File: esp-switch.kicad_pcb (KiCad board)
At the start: 2 copper layers, 23 parts, among them J1 Conn_01x02, J2 Screw_Terminal_01x02, J3 Screw_Terminal_01x02, J4 Conn_01x04, U1 ATTINY441-SSU, U2 ESP-01v090, U3 MOC3041M, U4 MOC3041M

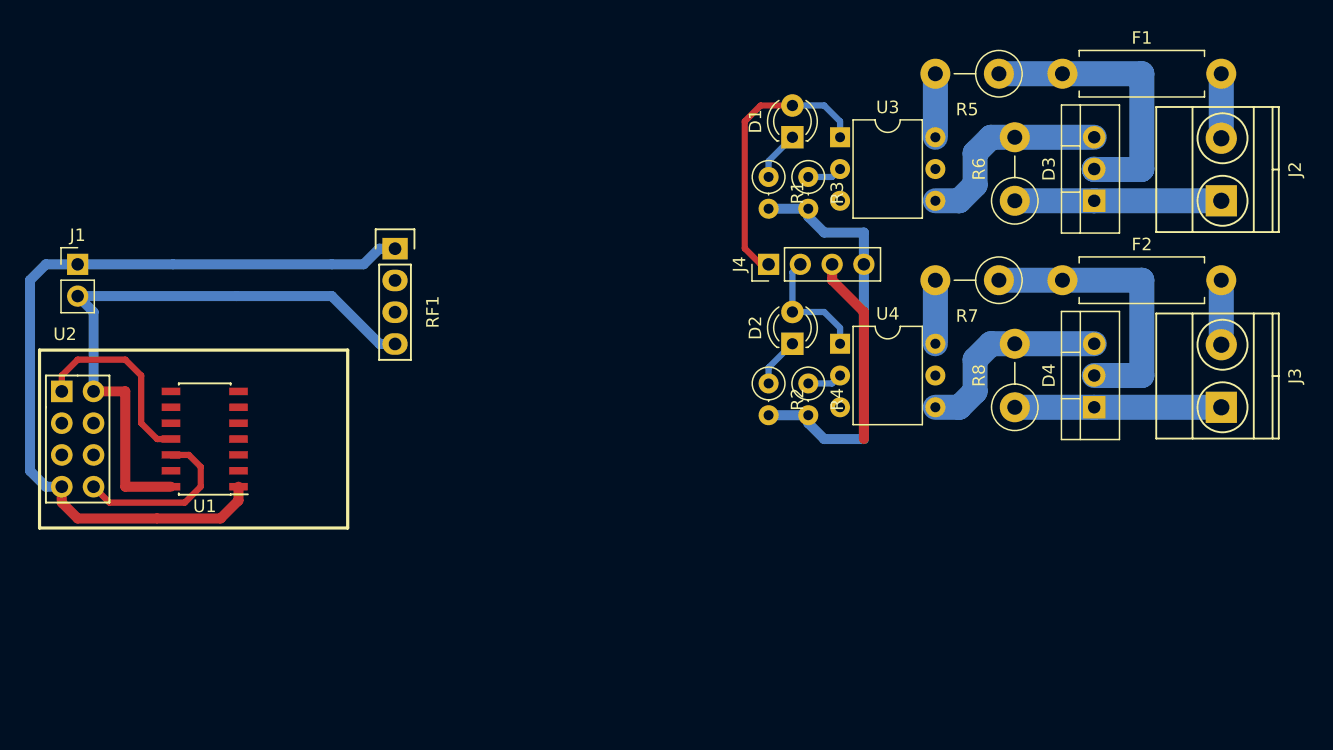
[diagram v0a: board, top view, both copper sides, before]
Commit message: Power supply added
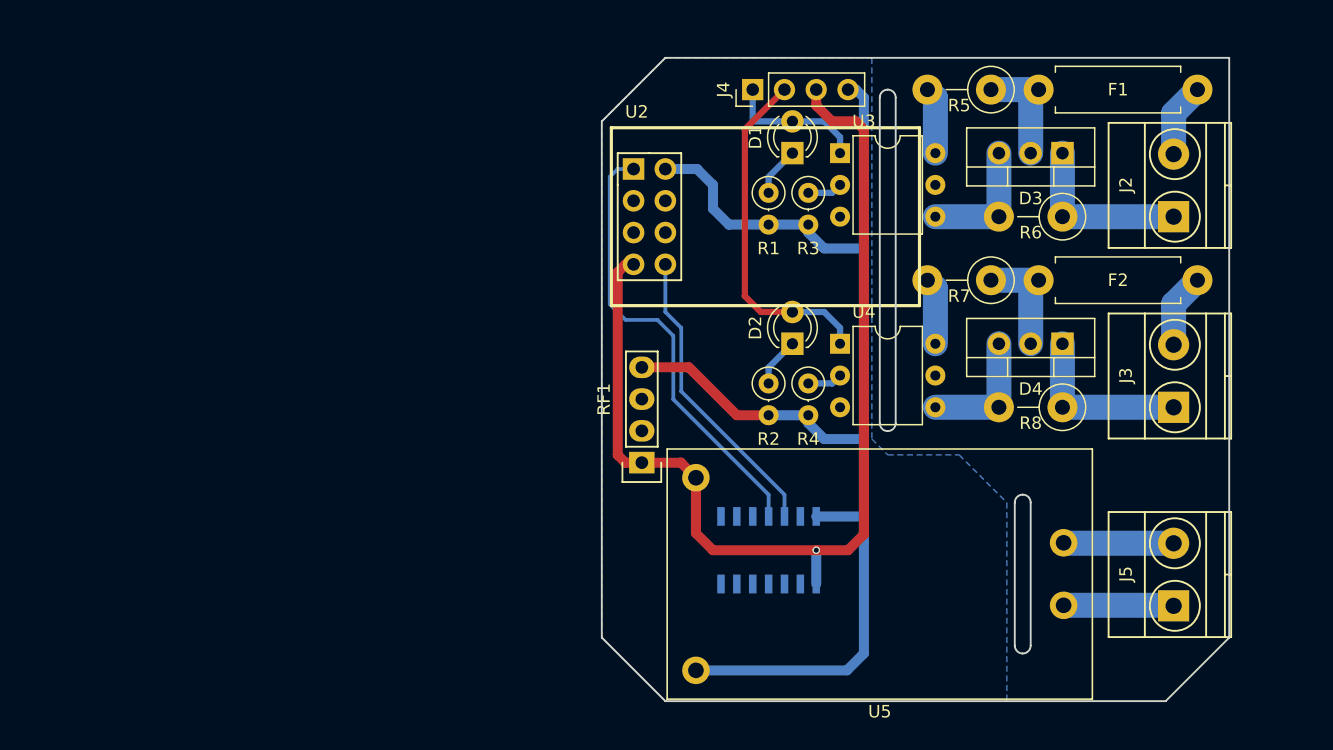
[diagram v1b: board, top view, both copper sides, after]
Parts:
- removed J1: Conn_01x02, Pin_Headers:Pin_Header_Straight_1x02_Pitch2.54mm
- added J5: Screw_Terminal_01x02, Connectors_Terminal_Blocks:TerminalBlock_Pheonix_MKDS1.5-2pol, F.Cu at (219.7, 136.5)
- added U5: HLK-PM05, Power_Supply:HLK-PM05, F.Cu at (196.2, 134.0)
- U1: moved to B.Cu
- moved U2 49.1 mm to (176.5, 101.6)
- moved U1 46.0 mm to (187.3, 132.1), turned to 90 degrees
- moved RF1 20.9 mm to (177.2, 120.0), turned to 90 degrees
- moved J4 14.0 mm to (186.1, 95.2)
- moved D4 5.68 mm to (210.8, 115.6), turned to 180 degrees
- moved D3 4.58 mm to (210.8, 100.3), turned to 180 degrees
- moved J2 4.02 mm to (219.7, 105.4)
- moved R6 4.02 mm to (210.8, 105.4), turned to 180 degrees
- moved J3 3.81 mm to (219.7, 120.7)
- moved R8 3.81 mm to (210.8, 120.7), turned to 180 degrees
- moved F1 2.29 mm to (208.9, 95.2)
- moved F2 1.91 mm to (208.9, 110.5)
- moved R5 1.42 mm to (205.1, 95.2)
- moved D1 1.27 mm to (189.2, 100.3)
- moved R1 1.27 mm to (187.3, 103.5)
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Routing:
- net GND: track 83.0 -> 104.4 mm
- net Net-(U1-Pad11): track 15.7 -> 36.1 mm
- net Net-(D2-Pad2): track 9.68 -> 27.8 mm
- net Net-(D3-Pad2): track 22.9 -> 9.15 mm
- net Net-(D4-Pad2): track 22.9 -> 9.15 mm
- net Net-(D1-Pad2): track 22.5 -> 11.3 mm
- net Net-(U1-Pad12): track 14.0 -> 24.1 mm
- net Net-(J5-Pad2): track 0.00 -> 8.81 mm
- net Net-(J5-Pad1): track 0.00 -> 8.81 mm
- net Net-(D3-Pad3): track 16.3 -> 10.2 mm
- net Net-(D4-Pad3): track 16.3 -> 10.2 mm
- net Net-(D3-Pad1): track 16.5 -> 14.0 mm
- net Net-(D4-Pad1): track 16.5 -> 14.0 mm
- net +5V: track 81.2 -> 83.1 mm, vias 0 -> 1
- net Net-(F2-Pad2): track 5.16 -> 5.95 mm
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- added copper zone on B.Cu, net GND
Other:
- board outline added: 50.2 x 51.4 mm
- net class Default: clearance 0.3 -> 0.2; trace_width 0.5 -> 0.3
- rule trace_clearance: 0.3 -> 0.2

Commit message: Single switch source
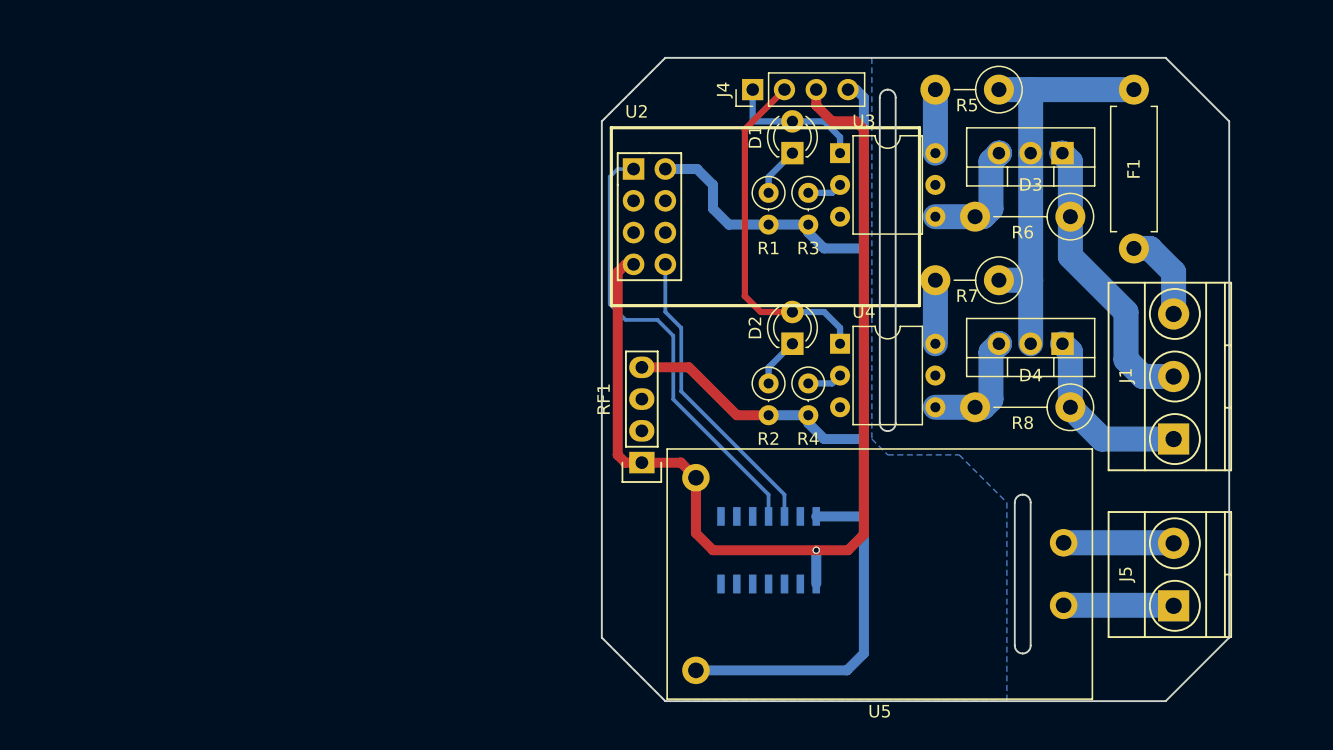
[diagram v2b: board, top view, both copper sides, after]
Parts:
- removed F2: Fuse_Small, Resistors_THT:R_Axial_DIN0411_L9.9mm_D3.6mm_P12.70mm_Horizontal
- removed J2, J3: Screw_Terminal_01x02, Connectors_Terminal_Blocks:TerminalBlock_Pheonix_MKDS1.5-2pol
- added J1: Screw_Terminal_01x03, Connectors_Terminal_Blocks:TerminalBlock_Pheonix_MKDS1.5-3pol, F.Cu at (219.7, 123.2)
- R6, R8: footprint Resistors_THT:R_Axial_DIN0411_L9.9mm_D3.6mm_P5.08mm_Vertical -> Resistors_THT:R_Axial_DIN0411_L9.9mm_D3.6mm_P7.62mm_Vertical
- moved F1 7.62 mm to (216.5, 95.2), turned to 270 degrees
- moved R5 0.64 mm to (205.7, 95.2)
- moved R6 0.64 mm to (211.5, 105.4)
- moved R7 0.64 mm to (205.7, 110.5)
- moved R8 0.64 mm to (211.5, 120.7)
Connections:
- D4 pad 2: Net-(D4-Pad2) -> Net-(D3-Pad2)
- R7 pad 1: Net-(D4-Pad2) -> Net-(D3-Pad2)
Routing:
- net Net-(D3-Pad2): track 9.15 -> 33.7 mm
- net Net-(D4-Pad2): track 9.15 -> 0.00 mm
- net Net-(D3-Pad1): track 14.0 -> 23.0 mm
- net Net-(F2-Pad2): track 5.95 -> 0.00 mm
- net Net-(F1-Pad2): track 5.95 -> 7.30 mm
- net Net-(D4-Pad1): track 14.0 -> 14.7 mm
- net Net-(D4-Pad3): track 10.2 -> 9.51 mm
- net Net-(D3-Pad3): track 10.2 -> 9.51 mm
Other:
- outline, holes or cut-outs redrawn

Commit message: Complete layout
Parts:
- added ?: MountingHole_2.7mm_M2.5, Mounting_Holes:MountingHole_2.7mm_M2.5, F.Cu at (217.2, 141.0)
- added ?: MountingHole_2.7mm_M2.5, Mounting_Holes:MountingHole_2.7mm_M2.5, F.Cu at (221.0, 99.7)
- added ?: MountingHole_2.7mm_M2.5, Mounting_Holes:MountingHole_2.7mm_M2.5, F.Cu at (175.9, 99.7)
- added J2: Conn_01x04, Pin_Headers:Pin_Header_Straight_1x04_Pitch2.54mm, B.Cu at (200.7, 129.5)
- RF1: value RF_Receiver_433_MHz -> RF_Receiver_EV1527; footprint Sensors:RF_Receiver_433_MHz -> footprints:RF_Receiver_Decoder
- moved U2 20.5 mm to (182.2, 121.3), turned to 90 degrees
- moved RF1 16.6 mm to (175.9, 136.5), turned to 180 degrees
- moved R2 11.3 mm to (184.2, 108.0), turned to 180 degrees
- moved R4 9.92 mm to (184.2, 111.1), turned to 180 degrees
- moved D2 7.73 mm to (188.0, 108.0), turned to 0 degrees
- moved J4 6.98 mm to (193.0, 95.2), turned to 270 degrees
- moved R3 6.35 mm to (184.2, 103.5), turned to 180 degrees
- moved U4 5.08 mm to (193.0, 110.5)
- moved R1 4.49 mm to (184.2, 100.3), turned to 180 degrees
- moved R7 2.54 mm to (208.3, 110.5)
- moved J5 1.91 mm to (219.7, 134.6)
- moved U1 1.80 mm to (188.6, 133.3)
- moved D1 1.27 mm to (188.0, 100.3), turned to 0 degrees
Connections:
- RF1 pad 1: +5V -> GND
- RF1 pad 2: Net-(RF1-Pad2) -> +5V
- RF1 pad 4: GND -> Net-(RF1-Pad4)
- U1 pad 10: Net-(U1-Pad10) -> Net-(RF1-Pad4)
- U1 pad 13: Net-(U1-Pad13) -> Net-(RF1-Pad3)
- U1 pad 2: Net-(U1-Pad2) -> Net-(D1-Pad2)
- U1 pad 3: Net-(U1-Pad3) -> Net-(D2-Pad2)
- U1 pad 5: Net-(U1-Pad5) -> Net-(RF1-Pad8)
- U1 pad 6: Net-(U1-Pad6) -> Net-(RF1-Pad7)
- U2 pad 3: Net-(U2-Pad3) -> +5V
- U2 pad 4: Net-(U2-Pad4) -> (no net)
- U2 pad 5: Net-(U2-Pad5) -> +5V
- U2 pad 6: Net-(U2-Pad6) -> (no net)
- U3 pad 3: Net-(U3-Pad3) -> (no net)
- U3 pad 5: Net-(U3-Pad5) -> (no net)
- U4 pad 3: Net-(U4-Pad3) -> (no net)
- U4 pad 5: Net-(U4-Pad5) -> (no net)
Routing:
- net +5V: track 83.1 -> 129.0 mm
- net Net-(D1-Pad2): track 11.3 -> 46.2 mm, vias 0 -> 1
- net Net-(RF1-Pad3): track 0.00 -> 28.1 mm
- net Net-(RF1-Pad8): track 0.00 -> 27.2 mm, vias 0 -> 1
- net Net-(D2-Pad2): track 27.8 -> 52.1 mm, vias 0 -> 1
- net Net-(J2-Pad1): track 0.00 -> 24.0 mm, vias 0 -> 1
- net Net-(J2-Pad2): track 0.00 -> 23.6 mm, vias 0 -> 1
- net Net-(RF1-Pad7): track 0.00 -> 23.4 mm, vias 0 -> 1
- net Net-(U1-Pad11): track 36.1 -> 14.2 mm
- net Net-(J2-Pad3): track 0.00 -> 18.9 mm, vias 0 -> 1
- net Net-(RF1-Pad4): track 0.00 -> 15.3 mm
- net Net-(J2-Pad4): track 0.00 -> 15.0 mm, vias 0 -> 1
- net Net-(U1-Pad12): track 24.1 -> 13.9 mm
- net Net-(R4-Pad1): track 2.80 -> 9.68 mm
- net Net-(R3-Pad1): track 2.80 -> 9.15 mm
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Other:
- board size 50.2 x 51.4 mm -> 51.4 x 51.4 mm
- board text added: "© Foxel 2018"

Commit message: Polishing
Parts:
- removed ? (x3): MountingHole_2.7mm_M2.5, Mounting_Holes:MountingHole_2.7mm_M2.5
- added REF**: MountingHole_2.7mm_M2.5_Pad, Mounting_Holes:MountingHole_2.7mm_M2.5_Pad, F.Cu at (175.8, 99.7)
- added REF**: MountingHole_2.7mm_M2.5_Pad, Mounting_Holes:MountingHole_2.7mm_M2.5_Pad, F.Cu at (216.9, 140.7)
- added REF**: MountingHole_2.7mm_M2.5_Pad, Mounting_Holes:MountingHole_2.7mm_M2.5_Pad, F.Cu at (221.0, 99.7)
- moved R5 2.54 mm to (208.3, 95.2)
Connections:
- U2 pad 4: (no net) -> Net-(J2-Pad1)
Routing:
- net Net-(J2-Pad1): track 24.0 -> 51.7 mm, vias 1 -> 2
- net Net-(R5-Pad2): track 5.08 -> 7.62 mm
- net Net-(D3-Pad2): track 31.1 -> 28.6 mm

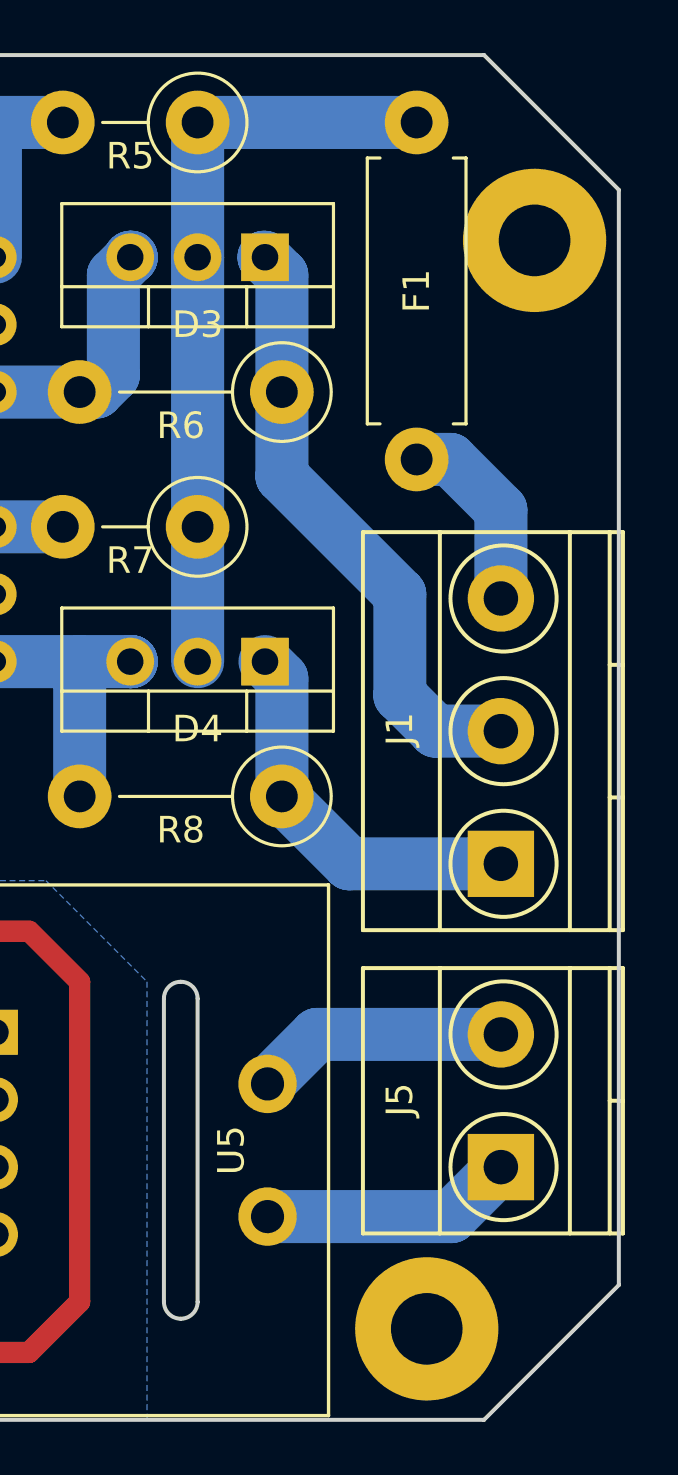
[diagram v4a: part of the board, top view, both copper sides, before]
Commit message: Power circuit fuse
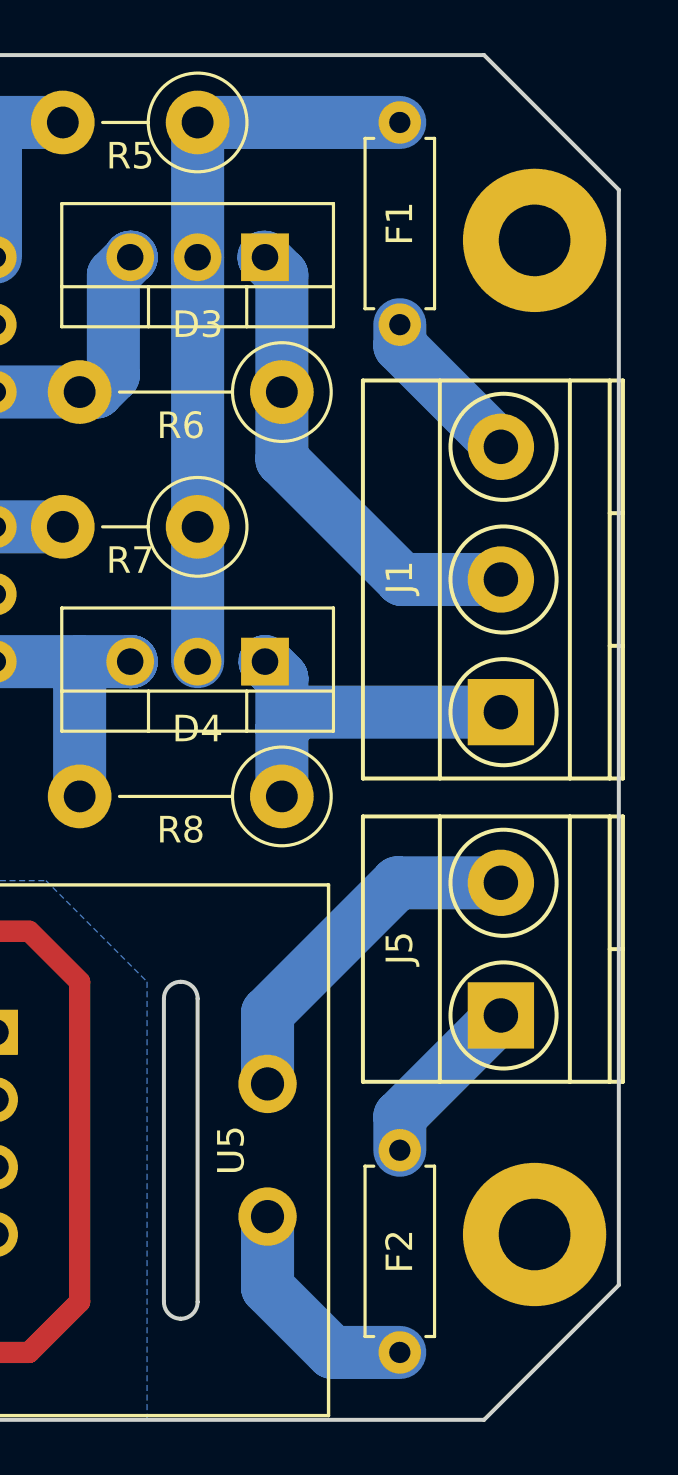
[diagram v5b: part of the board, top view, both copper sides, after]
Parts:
- added F2: Fuse_Small, Resistors_THT:R_Axial_DIN0207_L6.3mm_D2.5mm_P7.62mm_Horizontal, F.Cu at (215.9, 141.6)
- F1: footprint Resistors_THT:R_Axial_DIN0411_L9.9mm_D3.6mm_P12.70mm_Horizontal -> Resistors_THT:R_Axial_DIN0207_L6.3mm_D2.5mm_P7.62mm_Horizontal
- moved J1 5.72 mm to (219.7, 117.5)
- moved J5 5.72 mm to (219.7, 128.9)
- moved REF** 5.40 mm to (221.0, 137.2)
- moved F1 0.63 mm to (215.9, 95.2)
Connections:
- J5 pad 1: Net-(J5-Pad1) -> Net-(F2-Pad2)
- U5 pad 1: Net-(J5-Pad1) -> Net-(F2-Pad1)
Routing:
- net Net-(J5-Pad1): track 9.62 -> 0.00 mm
- net Net-(F2-Pad1): track 0.00 -> 8.73 mm
- net Net-(F2-Pad2): track 0.00 -> 6.66 mm
- net Net-(D3-Pad1): track 23.0 -> 18.1 mm
- net Net-(J5-Pad2): track 9.62 -> 13.6 mm
- net Net-(F1-Pad2): track 7.30 -> 6.18 mm
- net Net-(D3-Pad2): track 28.6 -> 27.9 mm

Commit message: Capasitor
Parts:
- added C1: CP_Small, Capacitors_THT:CP_Radial_D4.0mm_P2.00mm, F.Cu at (175.9, 135.9)
- moved RF1 5.08 mm to (175.9, 131.4)
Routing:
- net +5V: track 129.0 -> 139.1 mm
- net GND: track 103.7 -> 112.5 mm
- net Net-(RF1-Pad4): track 15.3 -> 20.1 mm
- net Net-(RF1-Pad7): track 23.4 -> 28.1 mm
- net Net-(RF1-Pad8): track 27.2 -> 32.0 mm
- net Net-(RF1-Pad3): track 28.1 -> 32.1 mm

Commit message: Copyright moved
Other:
- board text added: "© 2018 Foxel"
- board text removed: "© Foxel 2018"
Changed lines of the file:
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@@
     (links 57)
     (no_connects 0)
-    (area 172.644999 92.634999 224.230001 144.220001)
+    (area 163.410857 90.20238 240.26 153.195001)
     (thickness 1.6)
     (drawings 23)
@@
     )
   )
-  (gr_text "© Foxel\n2018" (at 184.15 114.935) (layer F.Cu)
-    (effects (font (size 1.5 1.5) (thickness 0.3)))
+  (gr_text "© 2018\nFoxel" (at 197.485 123.825) (layer B.SilkS)
+    (effects (font (size 1.5 1.5) (thickness 0.3)) (justify mirror))
   )
   (gr_line (start 196.215 120.015) (end 196.215 95.885) (angle 90) (layer Edge.Cuts) (width 0.15))
